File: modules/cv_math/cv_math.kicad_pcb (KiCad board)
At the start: 2 copper layers, 30.5 x 68.6 mm, 4 parts

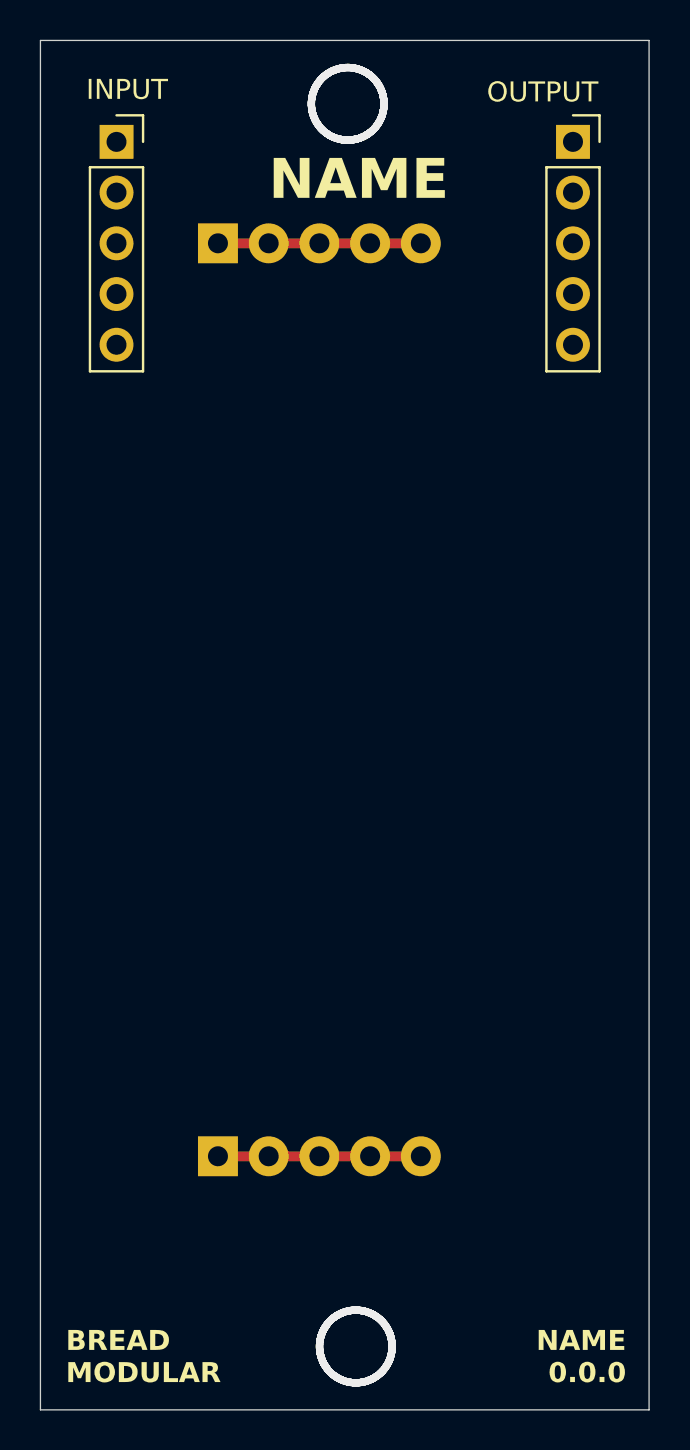
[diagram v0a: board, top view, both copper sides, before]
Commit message: Finished cv_math PCB routing
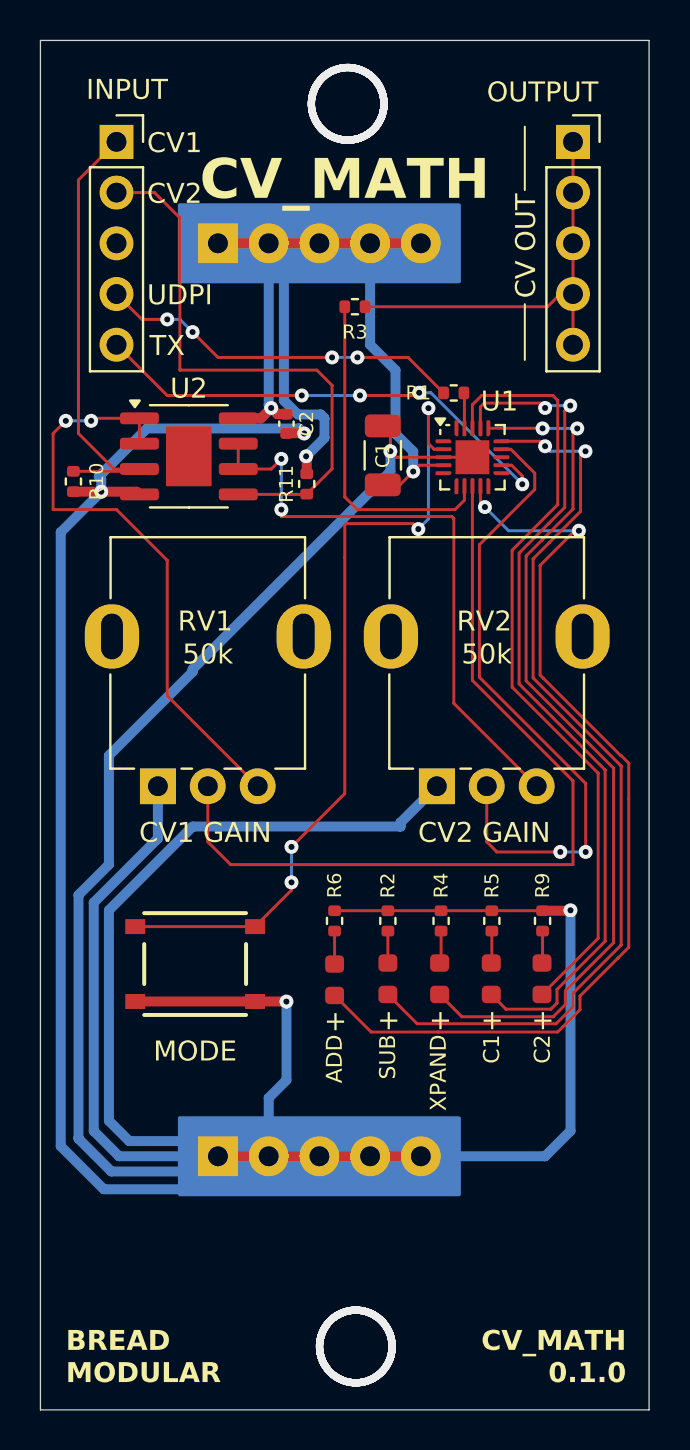
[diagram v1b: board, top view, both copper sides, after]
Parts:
- added C1: 100uf, Capacitor_SMD:C_1206_3216Metric, F.Cu at (64.1, 61.4)
- added C2: 0.1uf, Capacitor_SMD:C_0402_1005Metric, F.Cu at (59.3, 59.8)
- added D1: LED_MODE_1, LED_SMD:LED_0603_1608Metric, F.Cu at (64.4, 87.6)
- added D2: LED_MODE_2, LED_SMD:LED_0603_1608Metric, F.Cu at (67.0, 87.6)
- added D3: LED_MODE_3, LED_SMD:LED_0603_1608Metric, F.Cu at (69.6, 87.6)
- added D4: LED_MODE_0, LED_SMD:LED_0603_1608Metric, F.Cu at (61.7, 87.7)
- added D5: LED_MODE_4, LED_SMD:LED_0603_1608Metric, F.Cu at (72.1, 87.6)
- added MODE_TOGGLE1: SW_SPST, BreadModular_MISC:SPST_TS-1187A-B-A-B, F.Cu at (54.7, 86.9)
- added R1: 4.7k, Resistor_SMD:R_0402_1005Metric, F.Cu at (67.7, 58.3)
- added R10: 100k, Resistor_SMD:R_0402_1005Metric, F.Cu at (48.6, 62.7)
- added R11: 100k, Resistor_SMD:R_0402_1005Metric, F.Cu at (60.3, 62.9)
- added R2: 1k, Resistor_SMD:R_0402_1005Metric, F.Cu at (64.4, 84.7)
- added R3: 1k, Resistor_SMD:R_0402_1005Metric, F.Cu at (62.7, 54.0)
- added R4: 1k, Resistor_SMD:R_0402_1005Metric, F.Cu at (67.1, 84.7)
- added R5: 1k, Resistor_SMD:R_0402_1005Metric, F.Cu at (69.6, 84.7)
- added R6: 1k, Resistor_SMD:R_0402_1005Metric, F.Cu at (61.7, 84.7)
- added R9: 1k, Resistor_SMD:R_0402_1005Metric, F.Cu at (72.1, 84.7)
- added RV1: 50k, BreadModular_Pots:Potentiometer_RV09, F.Cu at (55.5, 71.0)
- added RV2: 50k, BreadModular_Pots:Potentiometer_RV09, F.Cu at (69.5, 71.0)
- added U1: ATtiny1616-M, Package_DFN_QFN:VQFN-20-1EP_3x3mm_P0.4mm_EP1.7x1.7mm, F.Cu at (68.6, 61.5)
- added U2: MCP6002-xSN, Package_SO:SOIC-8-1EP_3.9x4.9mm_P1.27mm_EP2.29x3mm, F.Cu at (54.4, 61.5)
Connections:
- INPUT1 pad 1: unconnected-(INPUT1-Pin_1-Pad1) -> CV1
- INPUT1 pad 2: unconnected-(INPUT1-Pin_2-Pad2) -> CV2
- INPUT1 pad 4: unconnected-(INPUT1-Pin_4-Pad4) -> UDPI
- INPUT1 pad 5: unconnected-(INPUT1-Pin_5-Pad5) -> TX
- OUTPUT1 pad 1: unconnected-(OUTPUT1-Pin_1-Pad1) -> CV_OUT
- OUTPUT1 pad 2: unconnected-(OUTPUT1-Pin_2-Pad2) -> CV_OUT
- OUTPUT1 pad 3: unconnected-(OUTPUT1-Pin_3-Pad3) -> CV_OUT
- OUTPUT1 pad 4: unconnected-(OUTPUT1-Pin_4-Pad4) -> CV_OUT
- OUTPUT1 pad 5: unconnected-(OUTPUT1-Pin_5-Pad5) -> CV_OUT
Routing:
- net GND: track 10.2 -> 232.8 mm, vias 0 -> 5
- net Net-(D4-A): track 0.00 -> 47.6 mm, vias 0 -> 2
- net Net-(D1-A): track 0.00 -> 46.4 mm, vias 0 -> 2
- net Net-(D2-A): track 0.00 -> 44.2 mm, vias 0 -> 2
- net Net-(D3-A): track 0.00 -> 43.3 mm, vias 0 -> 2
- net BUFF_CV1: track 0.00 -> 42.6 mm
- net V_SUPPLY: track 10.2 -> 51.2 mm, vias 0 -> 3
- net Net-(MODE_TOGGLE1-A): track 0.00 -> 40.7 mm, vias 0 -> 4
- net Net-(D5-A): track 0.00 -> 39.4 mm
- net BUFF_CV2: track 0.00 -> 32.4 mm, vias 0 -> 2
- net Net-(U2B--): track 0.00 -> 30.3 mm, vias 0 -> 2
- net Net-(U2A--): track 0.00 -> 29.7 mm, vias 0 -> 2
- net CV2: track 0.00 -> 28.7 mm
- net TX: track 0.00 -> 25.0 mm, vias 0 -> 4
- net CV1: track 0.00 -> 22.5 mm
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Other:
- board text added: "ADD"
- board text added: "C1"
- board text added: "C2"
- board text added: "CV OUT"
- board text added: "CV1"
- board text added: "CV1 GAIN"
- board text added: "CV2"
- board text added: "CV2 GAIN"
- board text added: "CV_MATH"
- board text added: "CV_MATH 0.1.0"
- board text added: "MODE"
- board text added: "SUB"
- board text added: "TX"
- board text added: "UDPI"
- board text added: "XPAND"
- board text removed: "NAME"
- board text removed: "NAME 0.0.0"
